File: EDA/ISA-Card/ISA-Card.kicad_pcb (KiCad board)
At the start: 2 copper layers, 138.4 x 98.4 mm, 161 parts, among them U7101 74HCT245, U7102 74HCT244, U7104 74HCT138, U7105 74HCT138, U7106 74LS08, U7107 74LS32, U7108 74LS32, U7109 74HC368, U7110 74HC04, U7111 74HC125, U7112 74HC74, U7113 74HC74, U7114 74HC4024, U7115 74HC4024, U7116 74HC595, U7117 74HC595, U7118 74HC595, U7119 8251, U7120 26LS31, U7121 26LS32, X2 Conn_02x04_Counter_Clockwise, X3 DB15_Female, X5 Conn_02x08_Counter_Clockwise

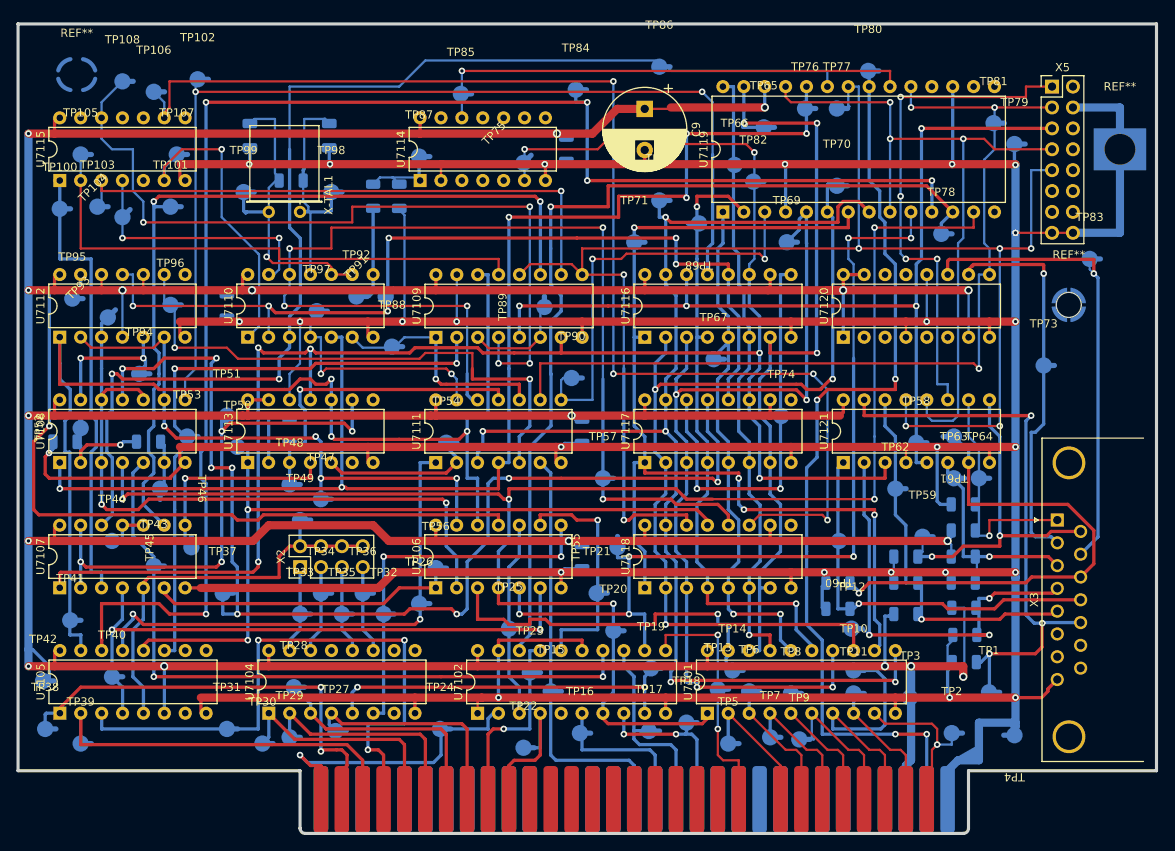
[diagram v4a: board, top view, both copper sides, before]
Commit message: Add extra silk screen markings, not fully acurate though
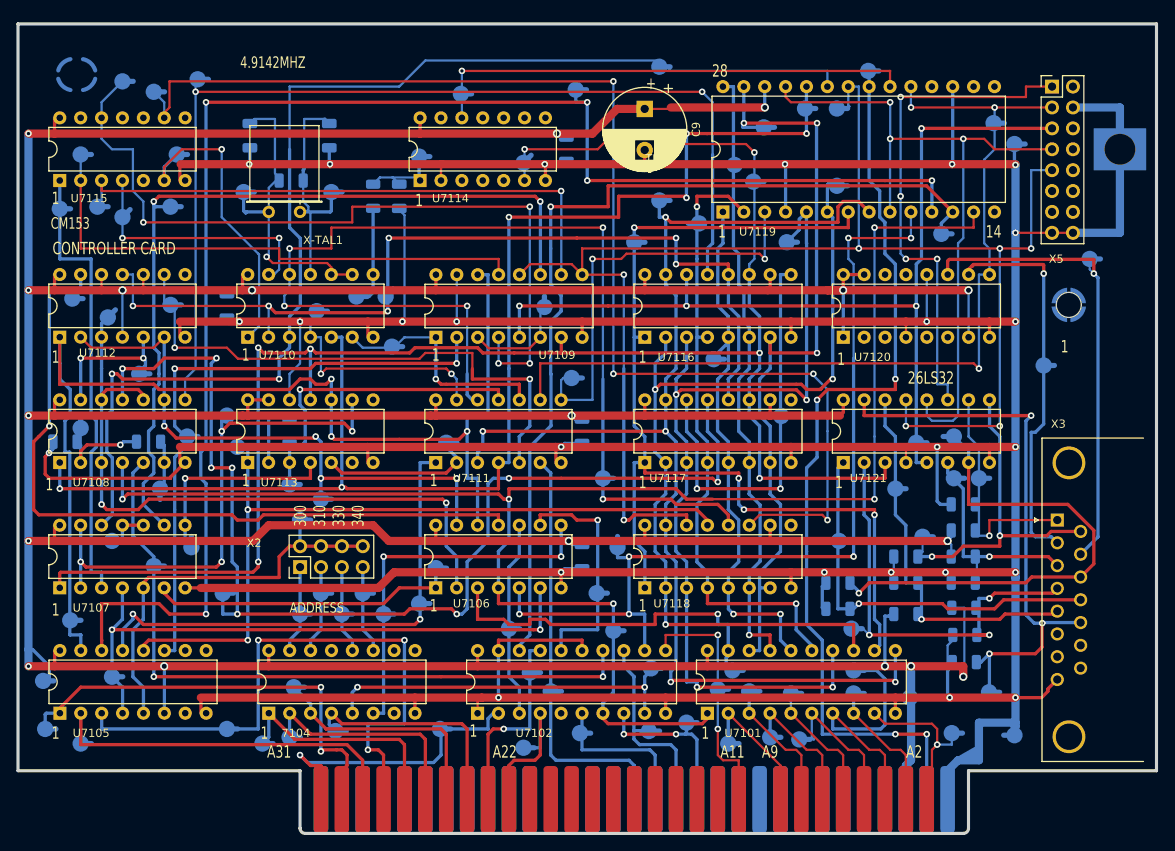
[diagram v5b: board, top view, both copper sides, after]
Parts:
- renumbered U7104 to 7104
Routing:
- net /D3: track 13.9 -> 16.3 mm
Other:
- board text added: "+"
- board text added: "-"
- board text added: "1"
- board text added: "14"
- board text added: "26LS32"
- board text added: "28"
- board text added: "300 310 330 340"
- board text added: "4.9142MHZ"
- board text added: "A11"
- board text added: "A2"
- board text added: "A22"
- board text added: "A31"
- board text added: "A9"
- board text added: "ADDRESS"
- board text added: "CM153"
- board text added: "CONTROLLER CARD"

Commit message: Change unseen traces under UART to connect data clocks and update unsure traces
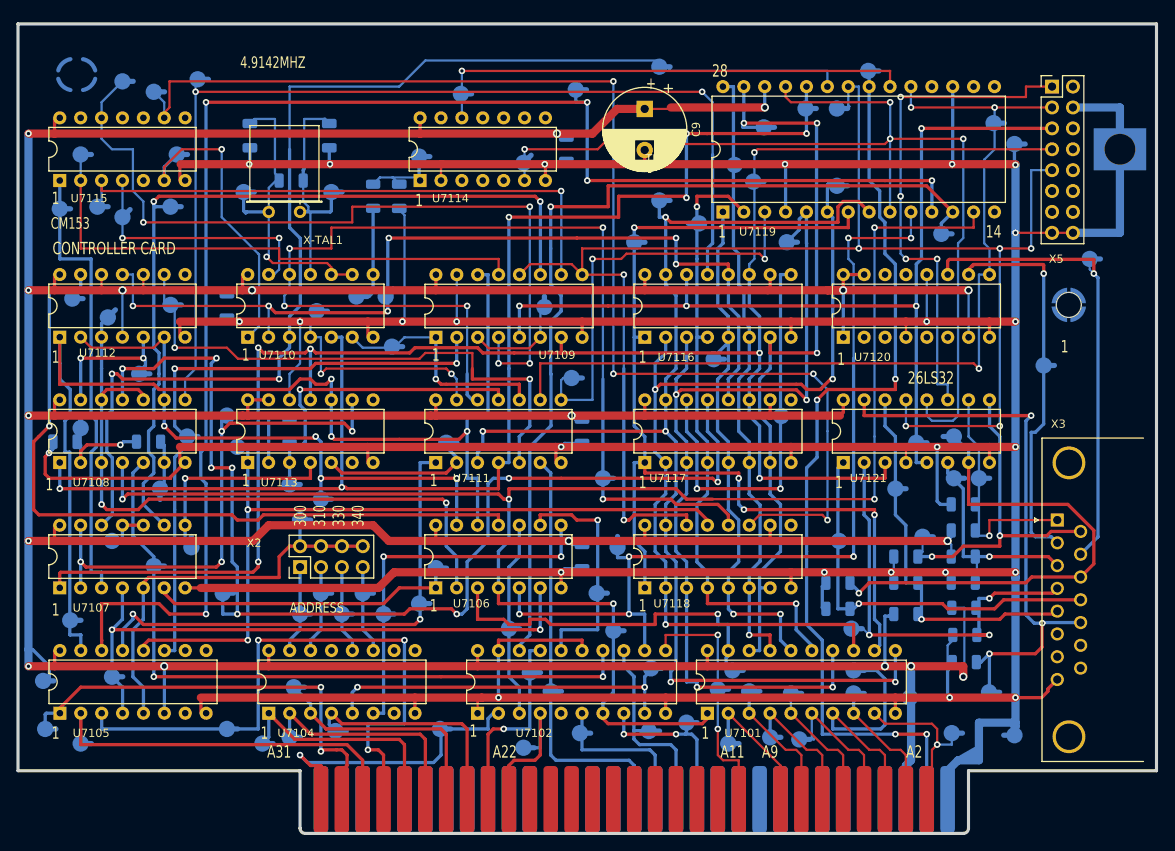
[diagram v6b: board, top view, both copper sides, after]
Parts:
- moved TP76 0.06 mm to (168.1, 61.7)
- renumbered 7104 to U7104
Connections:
- TP82 pad 1: /CLKp3 -> /Data Clock HV
- U7107 pad 1: /CLKp3 -> /Data Clock HV
- U7109 pad 7: /CLKp3 -> /Data Clock HV
- U7113 pad 11: /CLKp3 -> /Data Clock HV
- U7116 pad 11: /CLKp3 -> /Data Clock HV
- U7117 pad 11: /CLKp3 -> /Data Clock HV
- U7119 pad 25: /Data Clock LV -> /CLKp3
- U7119 pad 9: /Data Clock LV -> /CLKp3
- U7121 pad 12: /Data Clock LV -> /CLKp3
- U7121 pad 3: /CLKp3 -> /Data Clock HV
- X5 pad 7: /Data Clock LV -> /Data Clock HV
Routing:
- net /Data Clock HV: track 0.00 -> 218.1 mm, vias 0 -> 6
- net /CLKp3: track 216.0 -> 127.2 mm, vias 7 -> 4
- net /Data Clock LV: track 88.0 -> 0.00 mm, vias 3 -> 0

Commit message: Removed unused pads from ISA connector
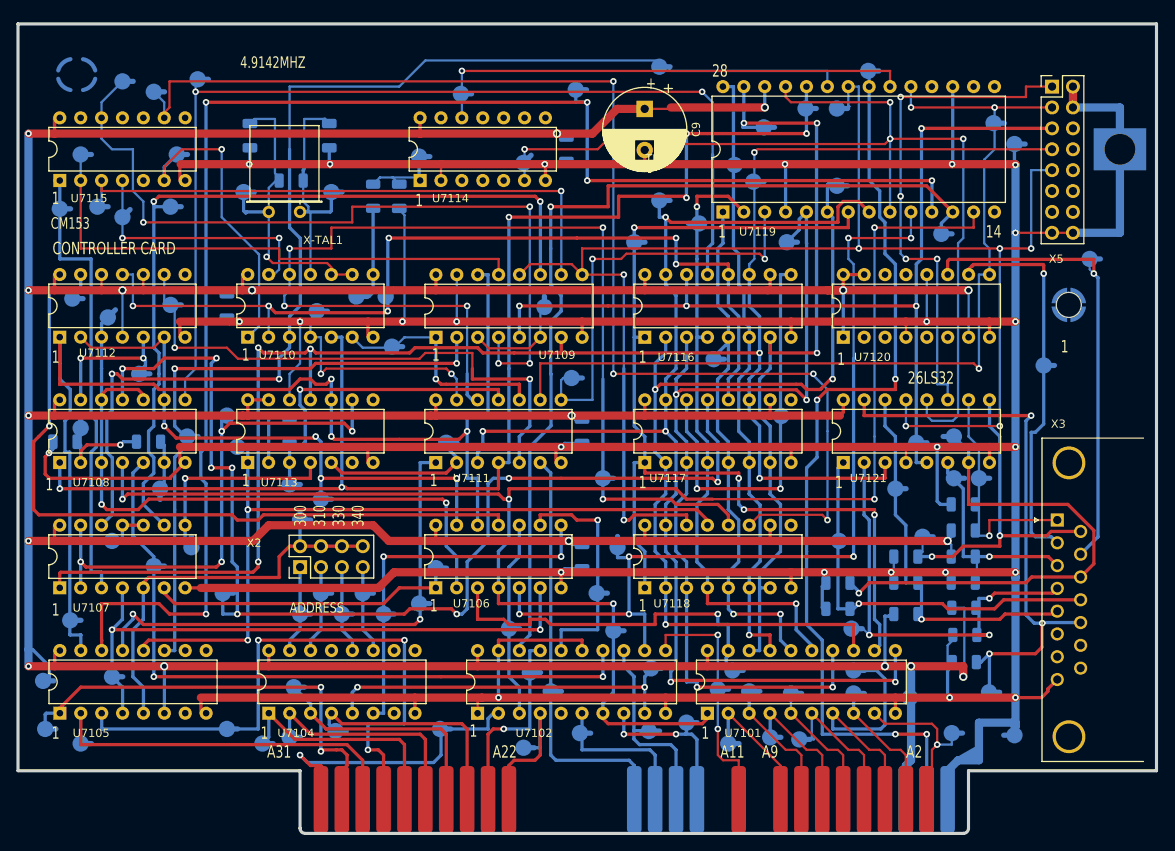
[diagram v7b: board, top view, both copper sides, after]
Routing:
- net unconnected-(BUS1-Pad9): track 2.86 -> 0.00 mm
- net GND: track 815.2 -> 817.8 mm

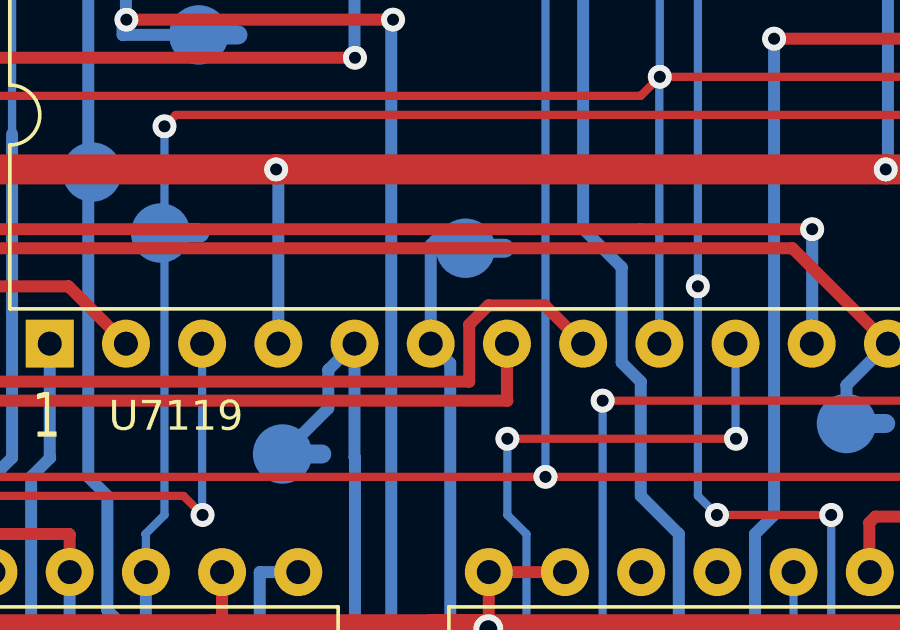
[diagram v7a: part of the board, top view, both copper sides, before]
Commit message: Connect Response to RXD
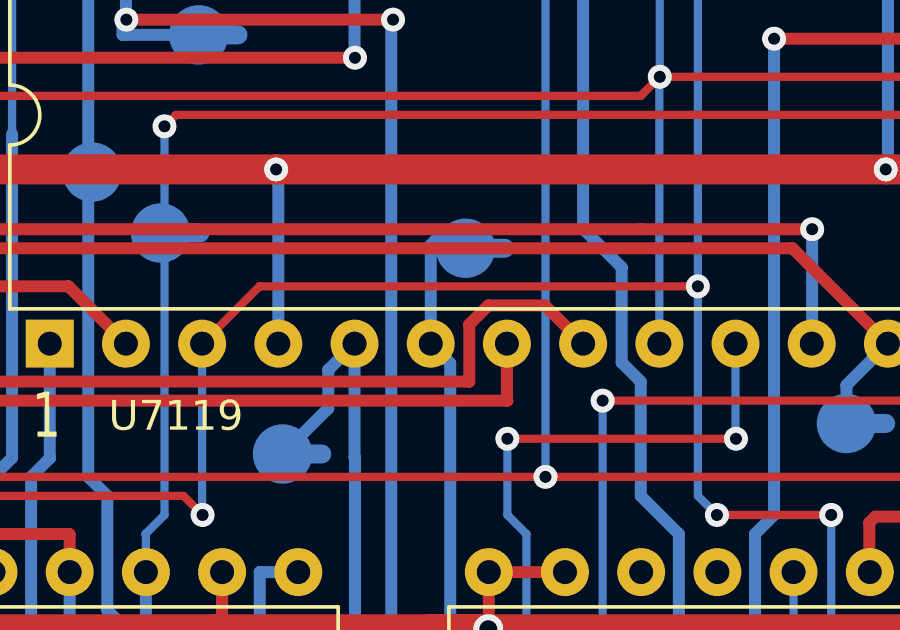
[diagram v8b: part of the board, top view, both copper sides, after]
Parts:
- C9: value C_Polarized -> 10uF
- R1: value R -> 10KΩ
- R2: value R -> 1MΩ
- R3: value R -> 100Ω
- R4: value R -> 1KΩ
- X-TAL1: value Crystal -> 4.9152MHz
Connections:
- net /Data Clock HV renamed /Data Clock
- net Net-(TP102-Pad1) renamed /U7116-~{OE}
- net Net-(TP37-Pad1) renamed /U7117-~{OE}
- net Net-(TP84-Pad1) renamed /UART-~{CS}
- net Net-(TP86-Pad1) renamed /~{RTS}
- TP90 pad 1: Net-(TP90-Pad1) -> /RXD
- U7111 pad 8: Net-(TP90-Pad1) -> /RXD
- U7119 pad 3: Net-(TP90-Pad1) -> /RXD
- U7121 pad 11: /Response -> /RXD
- X5 pad 1: /Response -> /RXD
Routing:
- net /RXD: track 0.00 -> 131.1 mm, vias 0 -> 6
- net /Response: track 61.9 -> 0.00 mm, vias 4 -> 0
- net Net-(TP90-Pad1): track 51.9 -> 0.00 mm, vias 2 -> 0
